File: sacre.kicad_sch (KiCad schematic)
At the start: 72 parts, among them IC1 ST25DV64KC-IE6S3, J1 USB_B_Micro, J2 Conn_01x24, J3 Con_BATT, M1 Vibration_Motor, Q1 DMP1045U_GSD, Q2 UMH3N, Q3 S8050, Q4 SI1308EDL, SW1 SW, SW2 SW, SW3 SW, SW4 SW, U1 TP4054, U2 ADP2108AUJ-3.3, U3 CP2104, U4 LIS3DH, U5 ESP32-PICO-D4, Y1 RV-8803-C7-TA-QC

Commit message: Clean KiCad project files
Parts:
- IC1: symbol SamacSys_Parts:ST25DV64KC-IE6S3 -> SmartFeedback-rescue:ST25DV64KC-IE6S3-SamacSys_Parts
- S1: footprint SamacSys_Parts:MSK12C02 -> MSK12C02:MSK12C02
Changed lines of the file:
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@@
       (effects (font (size 1.27 1.27)) (justify left))
     )
-    (property "Footprint" "SamacSys_Parts:MSK12C02" (id 2) (at 63.5 193.04 0)
+    (property "Footprint" "MSK12C02:MSK12C02" (id 2) (at 63.5 193.04 0)
       (effects (font (size 1.27 1.27)) (justify left) hide)
     )
@@
     (pin "1")
   )
-  (symbol (lib_id "SamacSys_Parts:ST25DV64KC-IE6S3") (at 144.78 176.53 180) (unit 1)
+  (symbol (lib_id "SmartFeedback-rescue:ST25DV64KC-IE6S3-SamacSys_Parts") (at 144.78 176.53 180) (unit 1)
     (in_bom yes) (on_board yes)
     (property "Reference" "IC1" (id 0) (at 123.19 183.261 0))
@@
     )
     (path "/00000000-0000-0000-0000-000060b23ba2"
-      (reference "S1") (unit 1) (value "MSK12C02") (footprint "SamacSys_Parts:MSK12C02")
+      (reference "S1") (unit 1) (value "MSK12C02") (footprint "MSK12C02:MSK12C02")
     )
     (path "/00000000-0000-0000-0000-00006040ab5e"

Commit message: Fix KiCad schematic symbol name
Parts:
- IC1: symbol SmartFeedback-rescue:ST25DV64KC-IE6S3-SamacSys_Parts -> SamacSys_Parts:ST25DV64KC-IE6S3
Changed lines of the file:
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@@
     (pin "1")
   )
-  (symbol (lib_id "SmartFeedback-rescue:ST25DV64KC-IE6S3-SamacSys_Parts") (at 144.78 176.53 180) (unit 1)
+  (symbol (lib_id "SamacSys_Parts:ST25DV64KC-IE6S3") (at 144.78 176.53 180) (unit 1)
     (in_bom yes) (on_board yes)
     (property "Reference" "IC1" (id 0) (at 123.19 183.261 0))

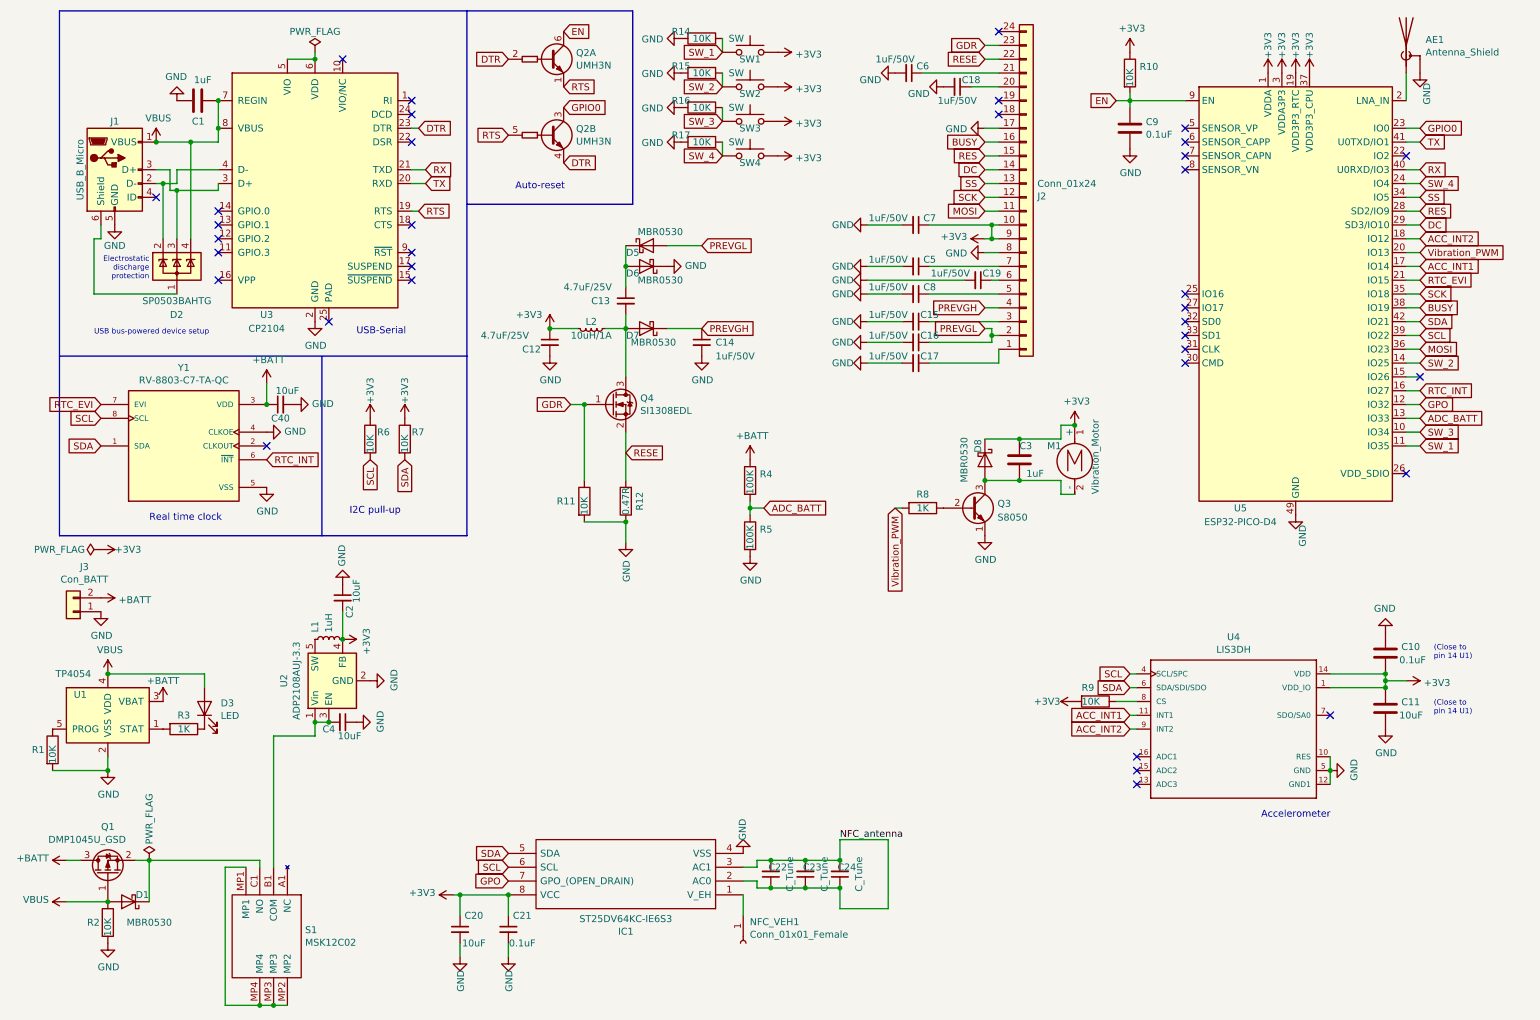
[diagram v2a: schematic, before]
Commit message: nuevas features: USB C, boton encendido, conector touch,sin botones, sin NFC
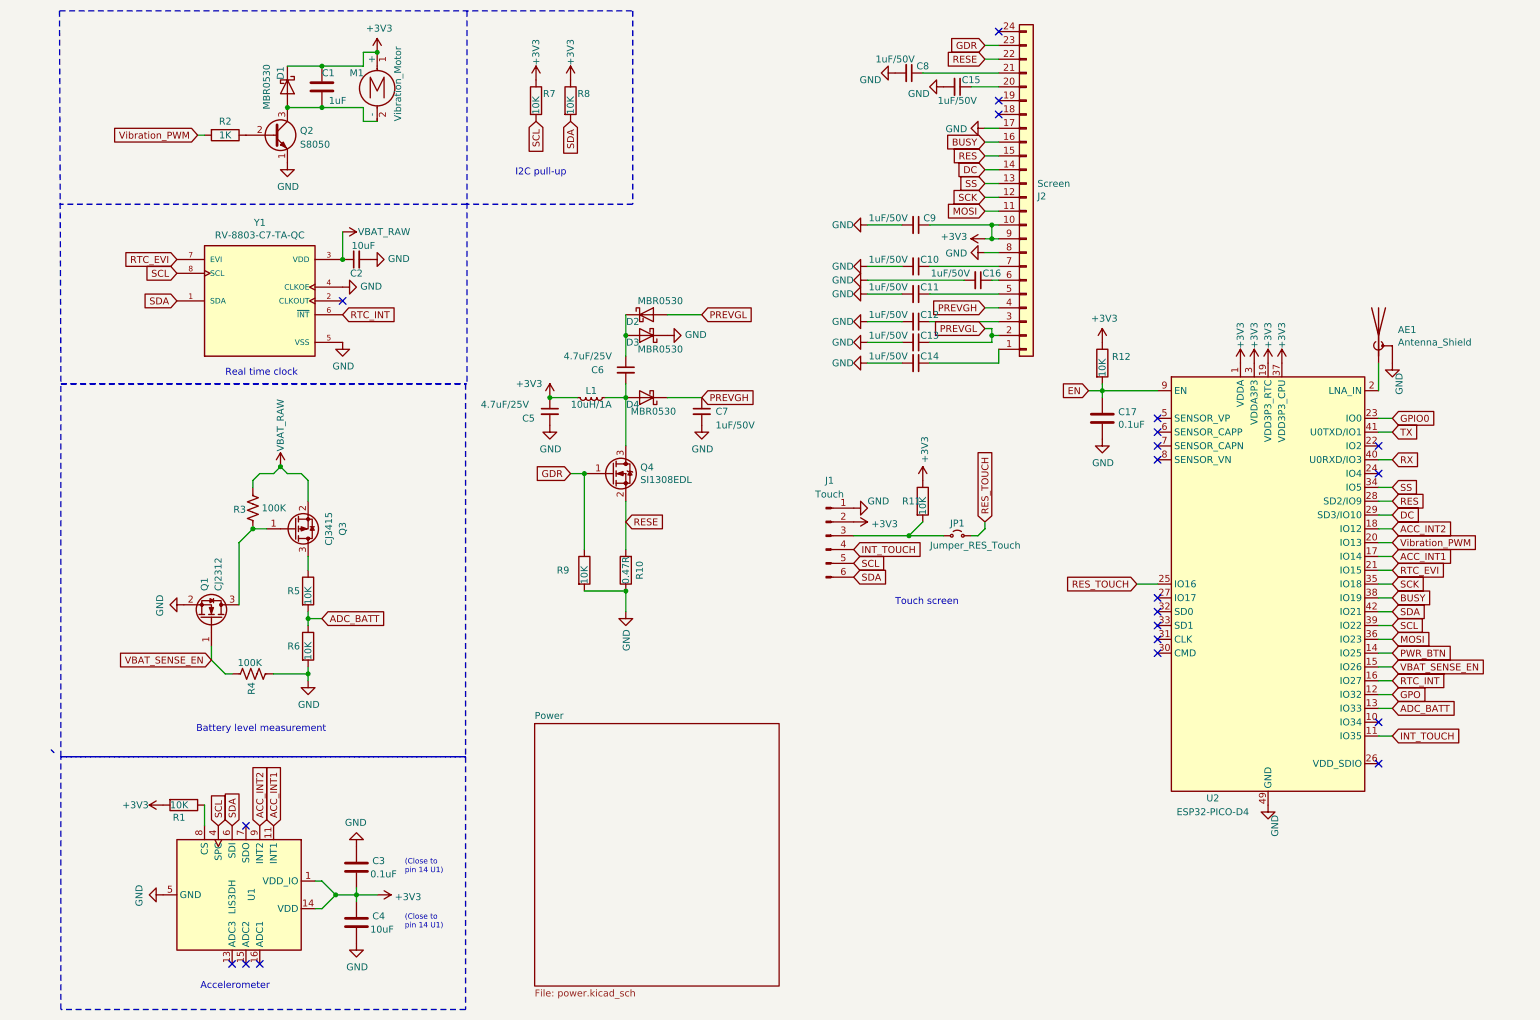
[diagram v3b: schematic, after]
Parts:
- removed C1: 1uF, Capacitor_SMD:C_0603_1608Metric, symbol SmartFeedback-rescue:C-Device
- removed C10: 0.1uF, Capacitor_SMD:C_0603_1608Metric, symbol SmartFeedback-rescue:C-Device
- removed C11: 10uF, Capacitor_SMD:C_0603_1608Metric, symbol SmartFeedback-rescue:C-Device
- removed C2, C20, C4: 10uF, Capacitor_SMD:C_0603_1608Metric, symbol SmartFeedback-rescue:C_Small-Device
- removed C21: 0.1uF, Capacitor_SMD:C_0603_1608Metric, symbol SmartFeedback-rescue:C_Small-Device
- removed C22, C23, C24: C_Tune, Capacitor_SMD:C_0603_1608Metric, symbol SmartFeedback-rescue:C_Small-Device
- removed D1: MBR0530, Diode_SMD:D_SOD-123, symbol SmartFeedback-rescue:MBR0530-Diode
- removed D2: SP0503BAHTG, Package_TO_SOT_SMD:SOT-143, symbol SmartFeedback-rescue:SP0503BAHT-Power_Protection
- removed D3: LED, LED_SMD:LED_1206_3216Metric_Pad1.42x1.75mm_HandSolder, symbol SmartFeedback-rescue:LED-Device
- removed IC1: ST25DV64KC-IE6S3, Package_SO:SO-8_3.9x4.9mm_P1.27mm, symbol SamacSys_Parts:ST25DV64KC-IE6S3
- removed J1: USB_B_Micro, Custom_USB:USB_Micro_CustomV2, symbol SmartFeedback-rescue:USB_B_Micro-Connector
- removed J3: Con_BATT, Connector_JST_Custom:JST_PH_S2B-PH-SM4-TB_1x02-1MP_P2.00mm_Horizontal, symbol SmartFeedback-rescue:Conn_01x02-Connector_Generic
- removed L1: 1uH, Inductor_SMD:L_0805_2012Metric_Pad1.15x1.40mm_HandSolder, symbol SmartFeedback-rescue:L_Small-Device
- removed NFC_VEH1: Conn_01x01_Female, Connector_PinHeader_2.00mm:PinHeader_1x01_P2.00mm_Vertical, symbol Connector:Conn_01x01_Female
- removed Q1: DMP1045U_GSD, Package_TO_SOT_SMD:SOT-23, symbol SmartFeedback-rescue:Q_PMOS_GSD-Device
- removed Q2: UMH3N, Package_TO_SOT_SMD:SOT-363_SC-70-6, symbol SmartFeedback-rescue:UMH3N-Transistor_BJT
- removed R14, R15, R16, R17, R2, R9: 10K, Resistor_SMD:R_0603_1608Metric, symbol SmartFeedback-rescue:R-Device
- removed R3: 1K, Resistor_SMD:R_0603_1608Metric, symbol SmartFeedback-rescue:R-Device
- removed R4: 100K, Resistor_SMD:R_0603_1608Metric, symbol SmartFeedback-rescue:R-Device
- removed S1: MSK12C02, MSK12C02:MSK12C02, symbol MSK12C02:MSK12C02
- removed SW1, SW2, SW3, SW4: SW, EVQ-PUA02K:EVQPUA02K, symbol SmartFeedback-rescue:SW_Push-Switch
- removed U1: TP4054, Package_TO_SOT_SMD:SOT-23-5, symbol SmartFeedback-rescue:MCP73831-2-OT-Battery_Management
- removed U2: ADP2108AUJ-3.3, Package_TO_SOT_SMD:TSOT-23-5, symbol SmartFeedback-rescue:ADP2108AUJ-3.3-Regulator_Switching
- removed U3: CP2104, Package_DFN_QFN:QFN-24-1EP_4x4mm_P0.5mm_EP2.6x2.6mm, symbol SmartFeedback-rescue:CP2104-Interface_USB
- removed U4: LIS3DH, LIS3DH:LGA-16_3x3mm_P0.5mm_LayoutBorder3x5y_custom, symbol LIS3DH:LIS3DH
- added C3: 0.1uF, Capacitor_SMD:C_0603_1608Metric, symbol SmartFeedback-rescue:C-Device
- added C4: 10uF, Capacitor_SMD:C_0603_1608Metric, symbol SmartFeedback-rescue:C-Device
- added J1: Touch, Connector_FFC-FPC:Hirose_FH12-6S-0.5SH_1x06-1MP_P0.50mm_Horizontal, symbol Connector:Conn_01x06_Pin
- added JP1: Jumper_RES_Touch, Jumper:SolderJumper-2_P1.3mm_Open_TrianglePad1.0x1.5mm, symbol Jumper:Jumper_2_Small_Open
- added Q1: CJ2312, Package_TO_SOT_SMD:SOT-23, symbol Transistor_FET:Q_NMOS_GSD
- added Q3: CJ3415, Package_TO_SOT_SMD:SOT-23, symbol Transistor_FET:Q_PMOS_GSD
- added R11, R6: 10K, Resistor_SMD:R_0603_1608Metric, symbol SmartFeedback-rescue:R-Device
- added R3, R4: 100K, Resistor_SMD:R_0603_1608Metric, symbol Device:R_US
- added U1: LIS3DH, Package_LGA:LGA-16_3x3mm_P0.5mm_LayoutBorder3x5y, symbol Sensor_Motion:LIS3DH
- J2: value Conn_01x24 -> Screen
- R5: value 100K -> 10K
- renumbered C3 to C1, C5 to C10, C8 to C11, C15 to C12, C16 to C13, C17 to C14, C18 to C15, C19 to C16, C9 to C17, C40 to C2, C12 to C5, C13 to C6, C14 to C7, C6 to C8, C7 to C9, D8 to D1, D5 to D2, D6 to D3, D7 to D4, L2 to L1, Q3 to Q2, R12 to R10, R10 to R12, R8 to R2, R6 to R7, R7 to R8, R11 to R9, U5 to U2
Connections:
- net +3V3: now also R1.2, C3.2, C4.1, J1.2 (Pin_2), R11.1, U1.1 (VDD_IO), U1.14 (VDD)
- net ACC_INT1: now also U1.11 (INT1)
- net ACC_INT2: now also U1.9 (INT2)
- net ADC_BATT: now also R5.2, R6.1; no longer R5.1
- net GND: now also C3.1, C4.2, J1.1 (Pin_1), Q1.2 (S), R4.1, R6.2, U1.10 (GND), U1.12 (GND), U1.5 (GND); no longer R1.2, R5.2
- net SCL: now also J1.5 (Pin_5), U1.4 (SPC)
- net SDA: now also J1.6 (Pin_6), U1.6 (SDI)
- net VBAT_SENSE_EN: now reaches U2.15 (IO26)
- net VBAT_SENSE_EN: now also Q1.1 (G), R4.2
- net RES_TOUCH: now reaches U2.25 (IO16)
- net RES_TOUCH: now also JP1.2 (B)
- net at R1.1: now also U1.8 (CS)
- net +BATT renamed VBAT_RAW
- net VBAT_RAW: now also Q3.2 (S), R3.2
- net SW_1 renamed INT_TOUCH
- net INT_TOUCH: now also J1.4 (Pin_4)
- net SW_2 renamed PWR_BTN
- net SW_3: no longer names the net of U2.10 (IO34)
- net SW_4: no longer names the net of U2.24 (IO4)
- new net: J1.3 (Pin_3), JP1.1 (A), R11.2
- new net: Q3.3 (D), R5.1
- new net: Q1.3 (D), Q3.1 (G), R3.1
- no-connect marks 36 -> 21
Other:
- added sheet Power (power.kicad_sch)
- note added: "Battery level measurement"
- note added: "Touch screen"
- note removed: "Auto-reset"
- note removed: "Electrostatic discharge protection"
- note removed: "USB bus-powered device setup"
- note removed: "USB-Serial"
- moved on the sheet: AE1, C1, C17, C2, C5, C6, C7, D1, D2, D3, D4, L1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

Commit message: se fini
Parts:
- M1: footprint Capacitor_SMD:C_1206_3216Metric_Pad1.42x1.75mm_HandSolder -> Capacitor_SMD:C_1206_3216Metric
- Q4: footprint Package_TO_SOT_SMD:SOT-323_SC-70_Handsoldering -> Package_TO_SOT_SMD:SOT-323_SC-70
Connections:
- net ANT_RF: now reaches AE1.1 (A), U2.2 (LNA_IN)
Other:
- moved on the sheet: AE1
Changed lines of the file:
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@@
 	(wire
 		(pts
-			(xy 261.62 78.74) (xy 261.62 83.82)
+			(xy 261.62 73.66) (xy 261.62 83.82)
 		)
 		(stroke
@@
 		)
 	)
+	(label "ANT_RF"
+		(at 261.62 80.01 90)
+		(fields_autoplaced yes)
+		(effects
+			(font
+				(size 1.27 1.27)
+			)
+			(justify left bottom)
+		)
+		(property "Clase de red" "antena"
+			(at 262.89 80.01 90)
+			(show_name no)
+			(do_not_autoplace no)
+			(effects
+				(font
+					(size 1.27 1.27)
+					(italic yes)
+				)
+				(justify left)
+			)
+		)
+	)
 	(global_label "SDA"
 		(shape input)
@@
 	(symbol
 		(lib_id "SmartFeedback-rescue:Antenna_Shield-Device")
-		(at 261.62 73.66 0)
+		(at 261.62 68.58 0)
 		(unit 1)
 		(body_style 1)
@@
 		(dnp no)
 		(property "Reference" "AE1"
-			(at 265.176 72.6186 0)
+			(at 265.176 67.5386 0)
 			(show_name no)
 			(do_not_autoplace no)
@@
 		)
 		(property "Value" "Antenna_Shield"
-			(at 265.176 74.93 0)
+			(at 265.176 69.85 0)
 			(show_name no)
 			(do_not_autoplace no)
@@
 		)
 		(property "Footprint" "Custom_antenna:AN012400C00R3200"
-			(at 261.62 71.12 0)
+			(at 261.62 66.04 0)
 			(hide yes)
 			(show_name no)
@@
 		)
 		(property "Datasheet" ""
-			(at 261.62 71.12 0)
+			(at 261.62 66.04 0)
 			(hide yes)
 			(show_name no)
@@
 		)
 		(property "Description" ""
-			(at 261.62 73.66 0)
+			(at 261.62 68.58 0)
 			(show_name no)
 			(do_not_autoplace no)
@@
 	(symbol
 		(lib_id "SmartFeedback-rescue:GND-power")
-		(at 264.16 78.74 0)
+		(at 264.16 73.66 0)
 		(unit 1)
 		(body_style 1)
@@
 		(dnp no)
 		(property "Reference" "#PWR044"
-			(at 264.16 85.09 0)
+			(at 264.16 80.01 0)
 			(hide yes)
 			(show_name no)
@@
 		)
 		(property "Value" "GND"
-			(at 265.43 82.55 90)
+			(at 265.43 77.47 90)
 			(show_name no)
 			(do_not_autoplace no)
@@
 		)
 		(property "Footprint" ""
-			(at 264.16 78.74 0)
+			(at 264.16 73.66 0)
 			(hide yes)
 			(show_name no)
@@
 		)
 		(property "Datasheet" ""
-			(at 264.16 78.74 0)
+			(at 264.16 73.66 0)
 			(hide yes)
 			(show_name no)
@@
 		)
 		(property "Description" ""
-			(at 264.16 78.74 0)
+			(at 264.16 73.66 0)
 			(show_name no)
 			(do_not_autoplace no)
@@
 			)
 		)
-		(property "Footprint" "Capacitor_SMD:C_1206_3216Metric_Pad1.42x1.75mm_HandSolder"
+		(property "Footprint" "Capacitor_SMD:C_1206_3216Metric"
 			(at 77.47 28.956 0)
 			(hide yes)
@@
 			)
 		)
-		(property "Footprint" "Package_TO_SOT_SMD:SOT-323_SC-70_Handsoldering"
+		(property "Footprint" "Package_TO_SOT_SMD:SOT-323_SC-70"
 			(at 125.73 96.52 0)
 			(hide yes)
@@
 		(dnp no)
 		(property "Reference" "R11"
-			(at 173.99 104.14 0)
+			(at 175.514 105.918 90)
 			(show_name no)
 			(do_not_autoplace no)
